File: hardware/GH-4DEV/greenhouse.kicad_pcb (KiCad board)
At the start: 2 copper layers, 200 x 100 mm, 171 parts, among them K1 OMRON G5LE, K2 OMRON G5LE, K3 OMRON G5LE, K4 OMRON G5LE, K5 OMRON G5LE, K6 OMRON G5LE, K7 OMRON G5LE, U1 PC847, U2 PC817, U3 MOC3052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

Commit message: fix: update hw to kicad 7, fix capacitor placement in 4.0dev
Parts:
- moved C19 22.2 mm to (166.4, 120.3), turned to 180 degrees
- moved R51 1.53 mm to (152.7, 118.4)
- moved X18 1.53 mm to (156.8, 118.4)
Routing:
- net GND: track 17.3 -> 13.8 mm, vias 209 -> 211
- net DIM0_CTRL: track 89.6 -> 88.1 mm
- net DIO0: track 86.9 -> 86.0 mm
- net +3V3: track 506.3 -> 505.4 mm
- net +5V: track 495.8 -> 496.6 mm
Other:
- board text added: "REV. 4.0-DEV"
- board text removed: "JLCJLCJLCJLC"
- board text removed: "REV. DEV4.0"

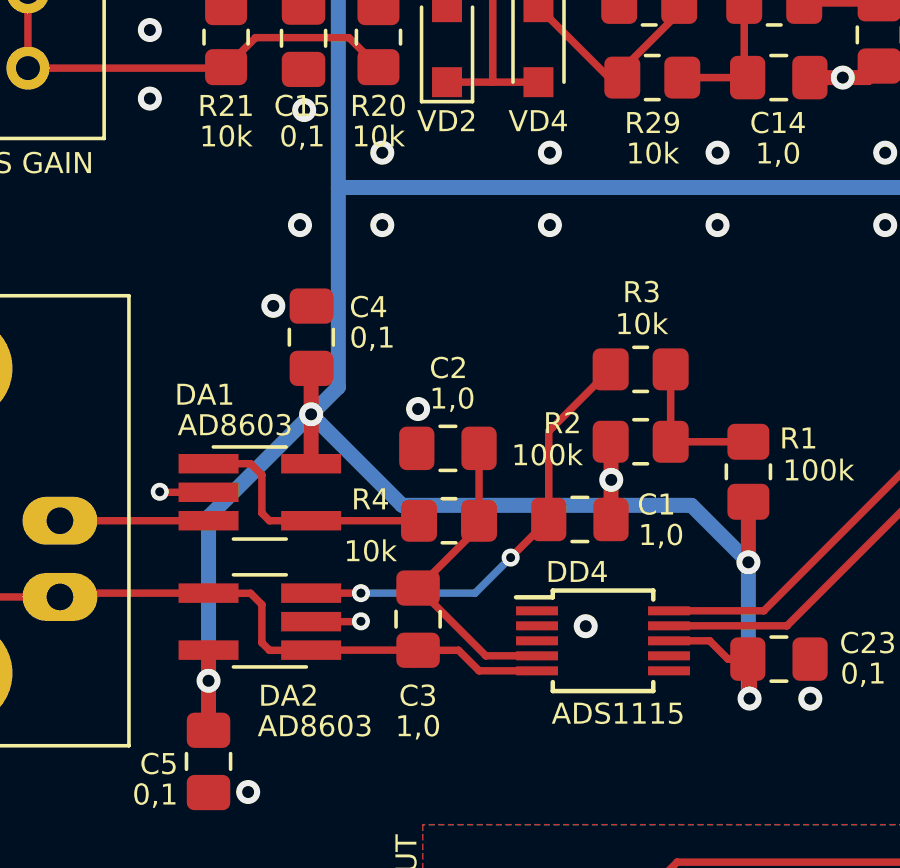
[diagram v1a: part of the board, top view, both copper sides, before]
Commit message: feat: add hw for tds & ph meters
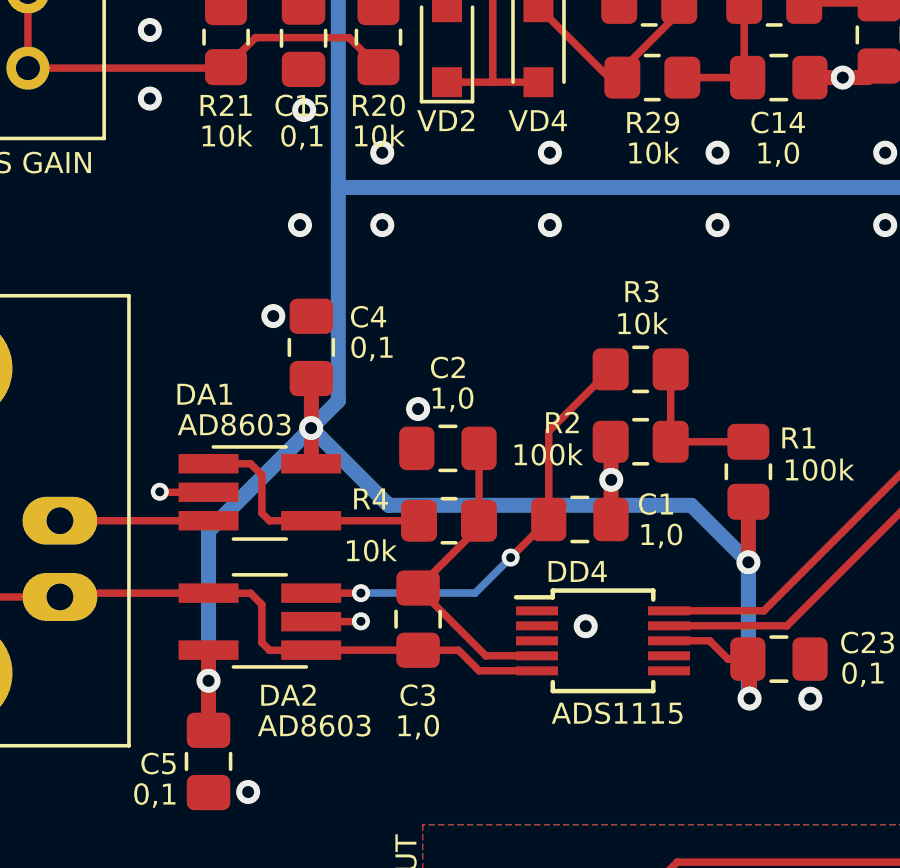
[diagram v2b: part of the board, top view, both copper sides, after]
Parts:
- moved C4 0.34 mm to (73.8, 109.1)
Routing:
- net +3V3: track 505.4 -> 504.9 mm
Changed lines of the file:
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@@
   )
   (footprint "Capacitor_SMD:C_0805_2012Metric_Pad1.18x1.45mm_HandSolder" (layer "F.Cu")
-    (at 73.8253 108.7737 90)
+    (at 73.8253 109.1135 90)
     (descr "Capacitor SMD 0805 (2012 Metric), square (rectangular) end terminal, IPC_7351 nominal with elongated pad for handsoldering. (Body size source: IPC-SM-782 page 76, https://www.pcb-3d.com/wordpress/wp-content/uploads/ipc-sm-782a_amendment_1_and_2.pdf, https://docs.google.com/spreadsheets/d/1BsfQQcO9C6DZCsRaXUlFlo91Tg2WpOkGARC1WS5S8t0/edit?usp=sharing), generated with kicad-footprint-generator")
     (tags "capacitor handsolder")
@@
   (via (at 183.2995 114.46) (size 0.8) (drill 0.4) (layers "F.Cu" "B.Cu") (net 1))
   (via (at 174.5365 119.604) (size 0.8) (drill 0.4) (layers "F.Cu" "B.Cu") (net 1))
-  (via (at 72.5555 107.7284) (size 0.8) (drill 0.4) (layers "F.Cu" "B.Cu") (net 1))
+  (via (at 72.5555 108.0682) (size 0.8) (drill 0.4) (layers "F.Cu" "B.Cu") (net 1))
   (via (at 188.9795 101.007) (size 0.8) (drill 0.4) (layers "F.Cu" "B.Cu") (net 1))
   (via (at 73.4445 105.036) (size 0.8) (drill 0.4) (layers "F.Cu" "B.Cu") (net 1))
@@
   (segment (start 62.3935 77.4816) (end 62.3935 79.0716) (width 0.5) (layer "F.Cu") (net 3))
   (segment (start 206.9215 107.103) (end 206.9125 107.094) (width 0.5) (layer "F.Cu") (net 3))
-  (segment (start 73.8163 112.9912) (end 73.8163 111.3442) (width 0.5) (layer "F.Cu") (net 3))
   (segment (start 73.5635 97.7716) (end 73.5635 96.7126) (width 0.5) (layer "F.Cu") (net 3))
   (segment (start 206.9215 111.294) (end 206.9215 107.103) (width 0.5) (layer "F.Cu") (net 3))
@@
   (segment (start 149.1685 84.592) (end 149.1685 83.472) (width 0.5) (layer "F.Cu") (net 3))
   (segment (start 150.3809 107.187411) (end 150.4065 107.161811) (width 0.5) (layer "F.Cu") (net 3))
+  (segment (start 73.8253 112.9822) (end 73.8163 112.9912) (width 0.5) (layer "F.Cu") (net 3))
   (segment (start 158.788504 100.743996) (end 150.4065 100.743996) (width 0.5) (layer "F.Cu") (net 3))
   (segment (start 146.5965 120.556) (end 146.5965 122.112) (width 0.5) (layer "F.Cu") (net 3))
@@
   (segment (start 198.0365 122.52) (end 198.0365 125.255) (width 0.5) (layer "F.Cu") (net 3))
   (segment (start 87.102207 118.893607) (end 85.746207 118.893607) (width 0.25) (layer "F.Cu") (net 3))
-  (segment (start 73.8163 111.3442) (end 73.8163 109.8202) (width 0.5) (layer "F.Cu") (net 3))
+  (segment (start 73.8253 110.151) (end 73.8253 112.9822) (width 0.5) (layer "F.Cu") (net 3))
   (segment (start 70.3963 120.2252) (end 70.3963 121.8762) (width 0.5) (layer "F.Cu") (net 3))
   (via (at 192.0365 113.52) (size 0.8) (drill 0.4) (layers "F.Cu" "B.Cu") (net 3))
@@
   (via (at 74.2825 95.9936) (size 0.8) (drill 0.4) (layers "F.Cu" "B.Cu") (net 3))
   (via (at 198.0365 116.52) (size 0.8) (drill 0.4) (layers "F.Cu" "B.Cu") (net 3))
-  (via (at 73.8163 111.3442) (size 0.8) (drill 0.4) (layers "F.Cu" "B.Cu") (net 3))
+  (via (at 73.8163 111.802) (size 0.8) (drill 0.4) (layers "F.Cu" "B.Cu") (net 3))
   (via (at 198.0365 113.52) (size 0.8) (drill 0.4) (layers "F.Cu" "B.Cu") (net 3))
   (via (at 192.0365 115.52) (size 0.8) (drill 0.4) (layers "F.Cu" "B.Cu") (net 3))
@@
   (via (at 234.8615 107.103) (size 0.8) (drill 0.4) (layers "F.Cu" "B.Cu") (net 3))
   (segment (start 72.5045 94.2156) (end 72.5045 84.3096) (width 0.5) (layer "B.Cu") (net 3))
-  (segment (start 76.850011 114.377911) (end 86.493811 114.377911) (width 0.5) (layer "B.Cu") (net 3))
   (segment (start 234.8615 107.103) (end 243.1595 107.103) (width 0.5) (layer "B.Cu") (net 3))
   (segment (start 114.2115 100.236) (end 114.2115 103.783) (width 0.5) (layer "B.Cu") (net 3))
@@
   (segment (start 109.1315 103.783) (end 109.1405 103.792) (width 0.5) (layer "B.Cu") (net 3))
   (segment (start 226.7015 90.301) (end 224.8505 92.152) (width 0.5) (layer "B.Cu") (net 3))
+  (segment (start 76.401411 114.377911) (end 86.493811 114.377911) (width 0.5) (layer "B.Cu") (net 3))
   (segment (start 151.6765 114.206) (end 153.9505 114.206) (width 0.5) (layer "B.Cu") (net 3))
   (segment (start 74.7227 103.783) (end 74.7227 96.4338) (width 0.5) (layer "B.Cu") (net 3))
   (segment (start 150.474311 107.094) (end 197.5095 107.094) (width 0.5) (layer "B.Cu") (net 3))
   (segment (start 150.3809 107.187411) (end 150.287489 107.094) (width 0.5) (layer "B.Cu") (net 3))
+  (segment (start 73.8163 111.802) (end 73.8163 111.8112) (width 0.5) (layer "B.Cu") (net 3))
   (segment (start 104.0515 103.783) (end 99.1407 103.783) (width 0.5) (layer "B.Cu") (net 3))
-  (segment (start 70.3963 114.7642) (end 70.3963 120.2252) (width 0.5) (layer "B.Cu") (net 3))
   (segment (start 226.6065 107.093989) (end 226.606489 107.094) (width 0.5) (layer "B.Cu") (net 3))
   (segment (start 226.606489 107.094) (end 219.6305 107.094) (width 0.5) (layer "B.Cu") (net 3))
@@
   (segment (start 150.4065 100.743996) (end 150.4065 97.696) (width 0.5) (layer "B.Cu") (net 3))
   (segment (start 219.5865 104.528) (end 219.6215 104.563) (width 0.5) (layer "B.Cu") (net 3))
+  (segment (start 70.3963 115.2312) (end 70.3963 120.2252) (width 0.5) (layer "B.Cu") (net 3))
   (segment (start 104.0515 100.236) (end 104.0515 103.783) (width 0.5) (layer "B.Cu") (net 3))
   (segment (start 88.3918 120.7803) (end 88.4305 120.819) (width 0.5) (layer "B.Cu") (net 3))
   (segment (start 104.0515 103.783) (end 104.0605 103.792) (width 0.5) (layer "B.Cu") (net 3))
   (segment (start 131.1025 107.094) (end 120.1805 107.094) (width 0.5) (layer "B.Cu") (net 3))
+  (segment (start 73.8163 111.802) (end 73.8255 111.802) (width 0.5) (layer "B.Cu") (net 3))
   (segment (start 219.5865 82.304) (end 219.5865 92.152) (width 0.5) (layer "B.Cu") (net 3))
   (segment (start 99.1407 103.783) (end 74.7227 103.783) (width 0.5) (layer "B.Cu") (net 3))
   (segment (start 109.1315 100.236) (end 109.1315 103.783) (width 0.5) (layer "B.Cu") (net 3))
-  (segment (start 86.493811 114.377911) (end 88.3918 116.2759) (width 0.5) (layer "B.Cu") (net 3))
   (segment (start 74.2825 95.9936) (end 72.5045 94.2156) (width 0.5) (layer "B.Cu") (net 3))
   (segment (start 114.2115 103.783) (end 114.2205 103.792) (width 0.5) (layer "B.Cu") (net 3))
@@
   (segment (start 72.5045 84.2386) (end 72.5045 84.3096) (width 0.5) (layer "B.Cu") (net 3))
   (segment (start 74.7227 96.4338) (end 74.2825 95.9936) (width 0.5) (layer "B.Cu") (net 3))
-  (segment (start 73.8163 111.3442) (end 70.3963 114.7642) (width 0.5) (layer "B.Cu") (net 3))
-  (segment (start 73.8163 111.3442) (end 74.7227 110.4378) (width 0.5) (layer "B.Cu") (net 3))
   (segment (start 78.6965 78.0466) (end 72.5045 84.2386) (width 0.5) (layer "B.Cu") (net 3))
   (segment (start 136.1825 120.556) (end 141.2625 120.556) (width 0.5) (layer "B.Cu") (net 3))
@@
   (segment (start 243.1595 107.103) (end 248.5365 101.726) (width 0.5) (layer "B.Cu") (net 3))
   (segment (start 131.1025 120.556) (end 136.1825 120.556) (width 0.5) (layer "B.Cu") (net 3))
-  (segment (start 73.8163 111.3442) (end 76.850011 114.377911) (width 0.5) (layer "B.Cu") (net 3))
+  (segment (start 73.8163 111.802) (end 74.7227 110.8956) (width 0.5) (layer "B.Cu") (net 3))
   (segment (start 98.9575 95.179) (end 98.9575 99.327) (width 0.5) (layer "B.Cu") (net 3))
   (segment (start 219.6305 107.094) (end 206.9125 107.094) (width 0.5) (layer "B.Cu") (net 3))
-  (segment (start 74.7227 110.4378) (end 74.7227 103.783) (width 0.5) (layer "B.Cu") (net 3))
   (segment (start 82.3935 78.0466) (end 78.6965 78.0466) (width 0.5) (layer "B.Cu") (net 3))
   (segment (start 150.287489 107.094) (end 131.1025 107.094) (width 0.5) (layer "B.Cu") (net 3))
   (segment (start 114.2205 103.792) (end 109.1405 103.792) (width 0.5) (layer "B.Cu") (net 3))
   (segment (start 234.8615 107.103) (end 234.852489 107.093989) (width 0.5) (layer "B.Cu") (net 3))
+  (segment (start 73.8163 111.8112) (end 70.3963 115.2312) (width 0.5) (layer "B.Cu") (net 3))
+  (segment (start 73.8255 111.802) (end 76.401411 114.377911) (width 0.5) (layer "B.Cu") (net 3))
+  (segment (start 74.7227 110.8956) (end 74.7227 103.783) (width 0.5) (layer "B.Cu") (net 3))
   (segment (start 98.9715 103.6138) (end 99.1407 103.783) (width 0.5) (layer "B.Cu") (net 3))
+  (segment (start 86.493811 114.377911) (end 88.3918 116.2759) (width 0.5) (layer "B.Cu") (net 3))
   (segment (start 224.8505 92.152) (end 219.5865 92.152) (width 0.5) (layer "B.Cu") (net 3))
   (segment (start 88.3918 116.2759) (end 88.3918 120.7803) (width 0.5) (layer "B.Cu") (net 3))

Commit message: Мелкие правки в железе и диммере
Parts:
- removed K7: OMRON G5LE, Relay_THT:Relay_SPDT_Omron-G5LE-1
- removed X14: RELAY6, TerminalBlock:TerminalBlock_bornier-3_P5.08mm
- added C38: 0,01/400V, Capacitor_THT:C_Rect_L13.0mm_W5.0mm_P10.00mm_FKS3_FKP3_MKS4, F.Cu at (241.3, 60.3)
- added HL9: STATUS1, LED_SMD:LED_0805_2012Metric_Pad1.15x1.40mm_HandSolder, F.Cu at (95.2, 82.6)
- added R60: 33, Resistor_THT:R_Axial_DIN0614_L14.3mm_D5.7mm_P20.32mm_Horizontal, F.Cu at (234.5, 50.3)
- added R61: 820, Resistor_SMD:R_0805_2012Metric_Pad1.20x1.40mm_HandSolder, F.Cu at (99.2, 85.3)
- added R62: 820, Resistor_SMD:R_0805_2012Metric_Pad1.20x1.40mm_HandSolder, F.Cu at (99.2, 82.6)
- added R64: 1,0, Resistor_THT:R_Axial_DIN0309_L9.0mm_D3.2mm_P2.54mm_Vertical, F.Cu at (204.0, 57.9)
- added R65: 1,0, Resistor_THT:R_Axial_DIN0309_L9.0mm_D3.2mm_P2.54mm_Vertical, F.Cu at (203.9, 54.0)
- added U4: MOC3052, Package_DIP:DIP-6_W7.62mm_LongPads, F.Cu at (241.6, 82.0)
- added VS2: BT139-600D, Package_TO_SOT_THT:TO-220-3_Vertical, F.Cu at (246.7, 60.4)
- added X19: DIMMER 1, TerminalBlock:TerminalBlock_bornier-2_P5.08mm, F.Cu at (239.6, 40.4)
- HL8: value RL6 -> STATUS0
- R50: value 10k -> 330
- R54: value 820 -> 330
- moved R50 117.4 mm to (237.7, 82.0)
- moved HL8 97.2 mm to (95.2, 85.3), turned to 0 degrees
- moved R54 51.6 mm to (240.6, 70.6), turned to 0 degrees
- moved R58 23.4 mm to (219.2, 70.7), turned to 0 degrees
- moved REF** 23.1 mm to (208.3, 71.1)
- moved U2 22.5 mm to (197.8, 69.3)
- moved R57 22.2 mm to (216.4, 82.0)
- moved U3 22.2 mm to (220.3, 82.0)
- moved VS1 22.2 mm to (225.3, 60.4)
- moved REF** 21.8 mm to (205.5, 41.1)
- moved X17 21.7 mm to (218.2, 40.4)
- moved R13 21.7 mm to (199.2, 46.7)
- moved X16 21.7 mm to (199.2, 40.4)
- moved R55 21.7 mm to (194.1, 46.7)
- moved VD1 21.6 mm to (202.5, 64.3)
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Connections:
- C35 pad 1: ACL -> Net-(R64-R)
- DA6 pad 10: /RLD6 -> unconnected-(DA6-7C-Pad10)
- DA6 pad 7: RL6 -> GND
- DD1 pad 37: unconnected-(DD1-Pad37) -> DIM1_CTRL
- DD2 pad 10: RL6 -> STATUS_LED0
- DD2 pad 11: unconnected-(DD2-Pad11) -> STATUS_LED1
- HL8 pad 1: /RLD6 -> GND
- HL8 pad 2: Net-(HL8-Pad2) -> Net-(HL8-A)
- R50 pad 1: RL6 -> DIM1_CTRL
- R50 pad 2: GND -> Net-(R50-R)
- R54 pad 1: +5V -> DIM1_OUT
- R54 pad 2: Net-(HL8-Pad2) -> Net-(R54-R)
- VS1 pad 1: ACL -> Net-(R64-R)
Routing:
- net /RLD6: track 87.7 -> 0.00 mm
- net DIM1_CTRL: track 0.00 -> 84.6 mm, vias 0 -> 1
- net DIM1_OUT: track 0.00 -> 47.1 mm
- net Net-(R65-R): track 0.00 -> 42.9 mm
- net ACN: track 28.0 -> 55.7 mm
- net +5V: track 496.6 -> 469.4 mm
- net RLCOM6: track 27.0 -> 0.00 mm
- net DIM0_CTRL: track 88.1 -> 64.2 mm
- net ACL: track 46.4 -> 25.4 mm
- net Net-(R64-R): track 0.00 -> 19.8 mm
- net STATUS_LED1: track 0.00 -> 18.1 mm, vias 0 -> 2
- net RL6: track 17.7 -> 0.00 mm
- net STATUS_LED0: track 0.00 -> 15.8 mm, vias 0 -> 2
- net DIM_ZC: track 68.6 -> 55.3 mm
- net RLNC6: track 13.2 -> 0.00 mm
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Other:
- outline, holes or cut-outs redrawn
- board text added: "ELECTRIC HAZARD"
- board text added: "REV. 4.0 DEV"
- board text added: "VD2-VD7 SD103AWS"
- board text removed: "REV. 4.0-DEV"
- board text removed: "VD2-VD7: SD103AWS"
